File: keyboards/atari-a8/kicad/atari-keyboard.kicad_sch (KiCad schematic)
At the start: 20 parts, among them J101 PLAYER 1, J102 PLAYER 2, J103 I2C DISPLAY, U101 Elite-C

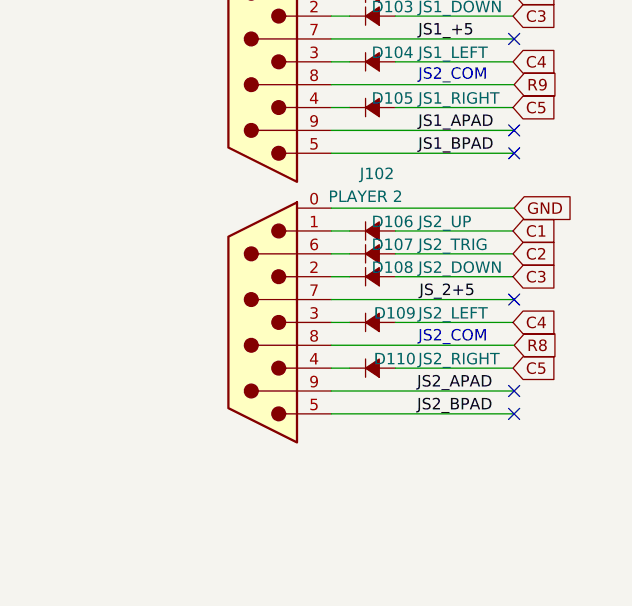
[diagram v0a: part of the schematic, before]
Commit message: Correct key sizes placed, diodes located, various auto-drawn stuff removed from PCB
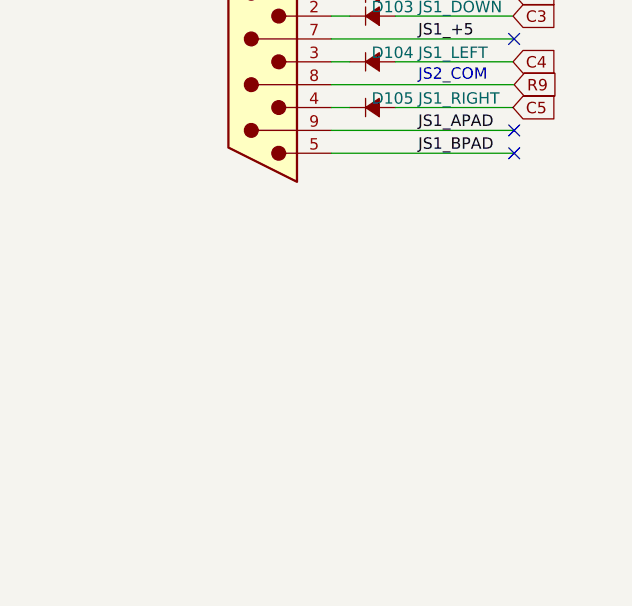
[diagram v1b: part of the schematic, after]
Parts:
- removed D106: JS2_UP, keebio:Diode-dual, symbol atari-keyboard-rescue:D_Small_ALT-Device
- removed D107: JS2_TRIG, retro-kbd:Diode-dual, symbol atari-keyboard-rescue:D_Small_ALT-Device
- removed D108: JS2_DOWN, retro-kbd:Diode-dual, symbol atari-keyboard-rescue:D_Small_ALT-Device
- removed D109: JS2_LEFT, retro-kbd:Diode-dual, symbol atari-keyboard-rescue:D_Small_ALT-Device
- removed D110: JS2_RIGHT, retro-kbd:Diode-dual, symbol atari-keyboard-rescue:D_Small_ALT-Device
- removed J102: PLAYER 2, Connector_Dsub:DSUB-9_Male_Horizontal_P2.77x2.84mm_EdgePinOffset9.90mm_Housed_MountingHolesOffset11.32mm, symbol jsconnector:DB9_Male
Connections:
- no-connect marks 11 -> 8

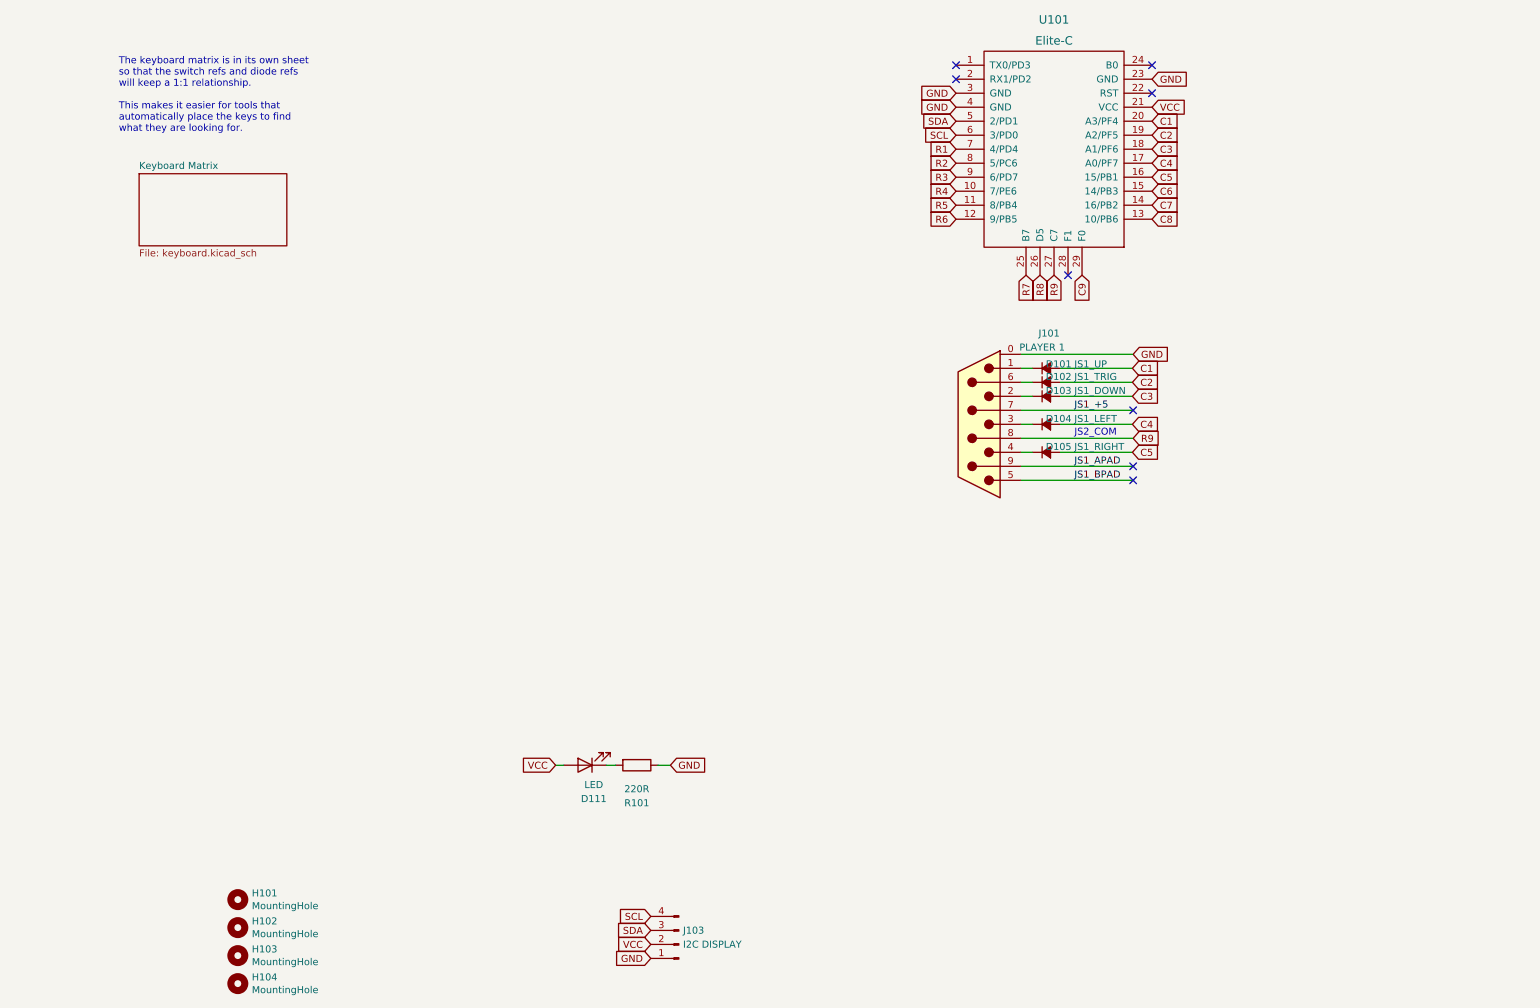
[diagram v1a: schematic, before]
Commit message: All global labels rendered. MAX7219's added. PCB updaed
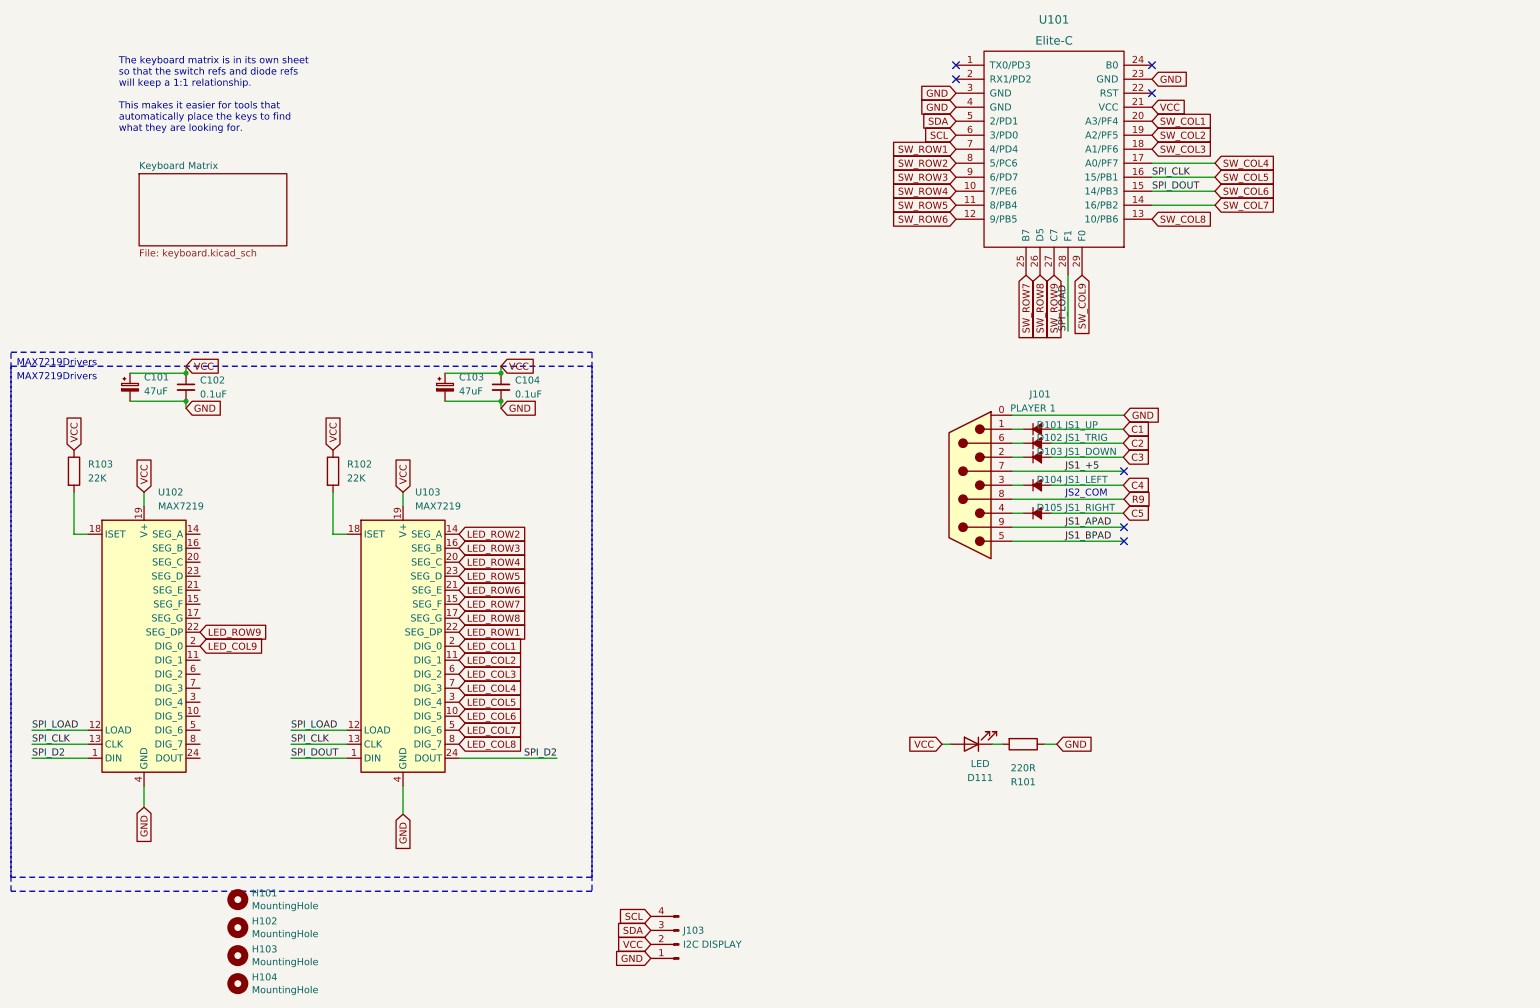
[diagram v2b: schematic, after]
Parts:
- added C101, C103: 47uF, Capacitor_THT:CP_Radial_D5.0mm_P2.50mm, symbol Device:C_Polarized_Small
- added C102, C104: 0.1uF, Capacitor_THT:C_Axial_L3.8mm_D2.6mm_P10.00mm_Horizontal, symbol Device:C_Small
- added R102, R103: 22K, keebio:Resistor-Hybrid, symbol Device:R
- added U102, U103: MAX7219, Package_DIP:DIP-24_W7.62mm_Socket_LongPads, symbol Driver_LED:MAX7219
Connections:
- net C1: no longer U101.20 (A3/PF4)
- net C2: no longer U101.19 (A2/PF5)
- net C3: no longer U101.18 (A1/PF6)
- net C4: no longer U101.17 (A0/PF7)
- net C5: no longer U101.16 (15/PB1)
- net GND: now also C101.2, C102.2, C103.2, C104.2, U102.4 (GND), U102.9 (GND), U103.4 (GND), U103.9 (GND)
- net R9: no longer U101.27 (C7)
- net VCC: now also C101.1, C102.1, C103.1, C104.1, R102.1, R103.1, U102.19 (V+), U103.19 (V+)
- net SPI_LOAD: now reaches U101.28 (F1)
- net SPI_LOAD: now also U102.12 (LOAD), U103.12 (LOAD)
- net C6 renamed SW_COL6
- net SW_COL6: now also U103.1 (DIN)
- net C7 renamed SW_COL7
- net C8 renamed SW_COL8
- net C9 renamed SW_COL9
- net R1 renamed SW_ROW1
- net R2 renamed SW_ROW2
- net R3 renamed SW_ROW3
- net R4 renamed SW_ROW4
- net R5 renamed SW_ROW5
- net R6 renamed SW_ROW6
- net R7 renamed SW_ROW7
- net R8 renamed SW_ROW8
- new net: R102.2, U103.18 (ISET)
- new net: R103.2, U102.18 (ISET)
- new net LED_COL1: U103.2 (DIG_0)
- new net LED_COL2: U103.11 (DIG_1)
- new net LED_COL3: U103.6 (DIG_2)
- new net LED_COL4: U103.7 (DIG_3)
- new net LED_COL5: U103.3 (DIG_4)
- new net LED_COL6: U103.10 (DIG_5)
- new net LED_COL7: U103.5 (DIG_6)
- new net LED_COL8: U103.8 (DIG_7)
- new net LED_COL9: U102.2 (DIG_0)
- new net LED_ROW1: U103.22 (SEG_DP)
- new net LED_ROW2: U103.14 (SEG_A)
- new net LED_ROW3: U103.16 (SEG_B)
- new net LED_ROW4: U103.20 (SEG_C)
- new net LED_ROW5: U103.23 (SEG_D)
- new net LED_ROW6: U103.21 (SEG_E)
- new net LED_ROW7: U103.15 (SEG_F)
- new net LED_ROW8: U103.17 (SEG_G)
- new net LED_ROW9: U102.22 (SEG_DP)
- new net SPI_D2: U102.1 (DIN), U103.24 (DOUT)
- new net SW_COL1: U101.20 (A3/PF4)
- new net SW_COL2: U101.19 (A2/PF5)
- new net SW_COL3: U101.18 (A1/PF6)
- new net SW_COL4: U101.17 (A0/PF7)
- new net SW_COL5: U101.16 (15/PB1), U102.13 (CLK), U103.13 (CLK)
- new net SW_ROW9: U101.27 (C7)
- no-connect marks 8 -> 7
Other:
- moved on the sheet: D101, D102, D103, D104, D105, D111, J101, R101

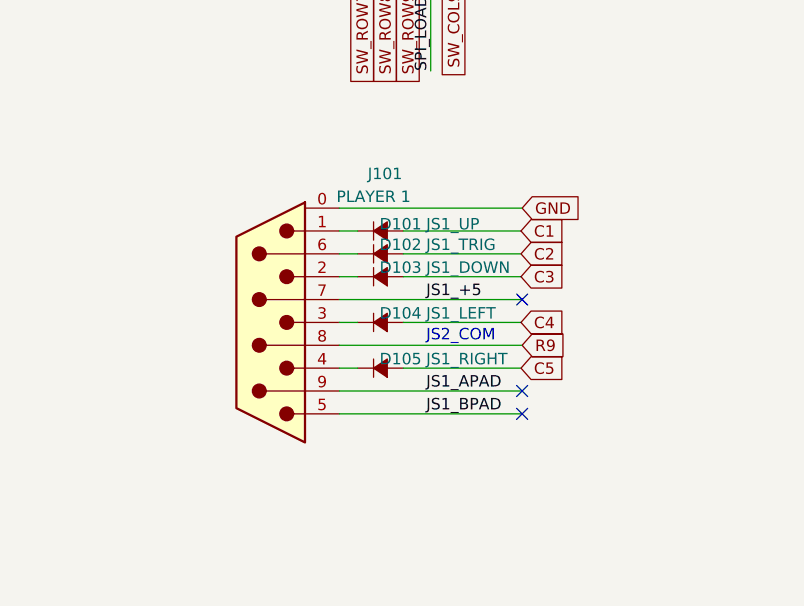
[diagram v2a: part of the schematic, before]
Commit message: Fixed joystick wiring
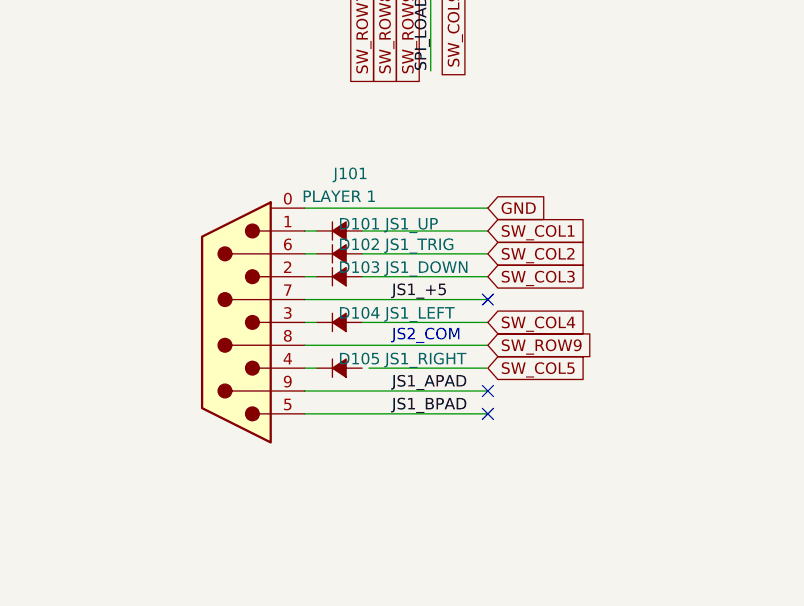
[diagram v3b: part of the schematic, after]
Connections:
- net C1 is gone; now on net SW_COL1: D101.2 (A)
- net C2 is gone; now on net SW_COL2: D102.2 (A)
- net C3 is gone; now on net SW_COL3: D103.2 (A)
- net C4 is gone; now on net SW_COL4: D104.2 (A)
- net R9 is gone; now on net SW_ROW9: J101.8
- net C5: no longer names the net of D105.2 (A)
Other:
- moved on the sheet: D101, D102, D103, D104, D105, J101

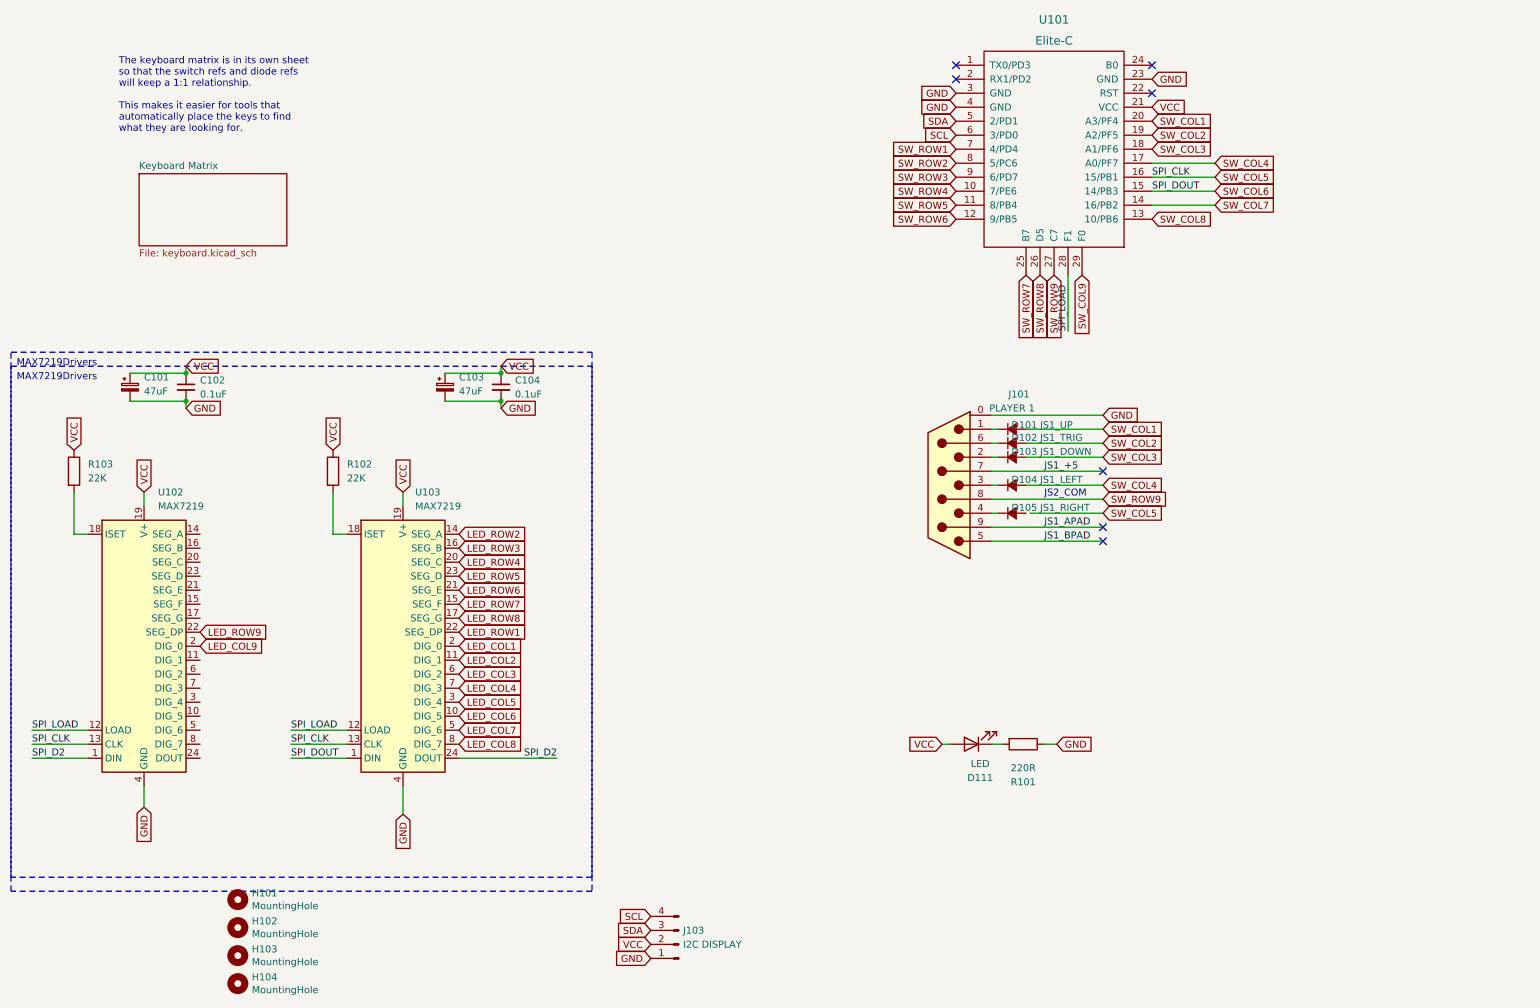
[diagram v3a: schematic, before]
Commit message: Added some tweaks learned working on keyboard prototype
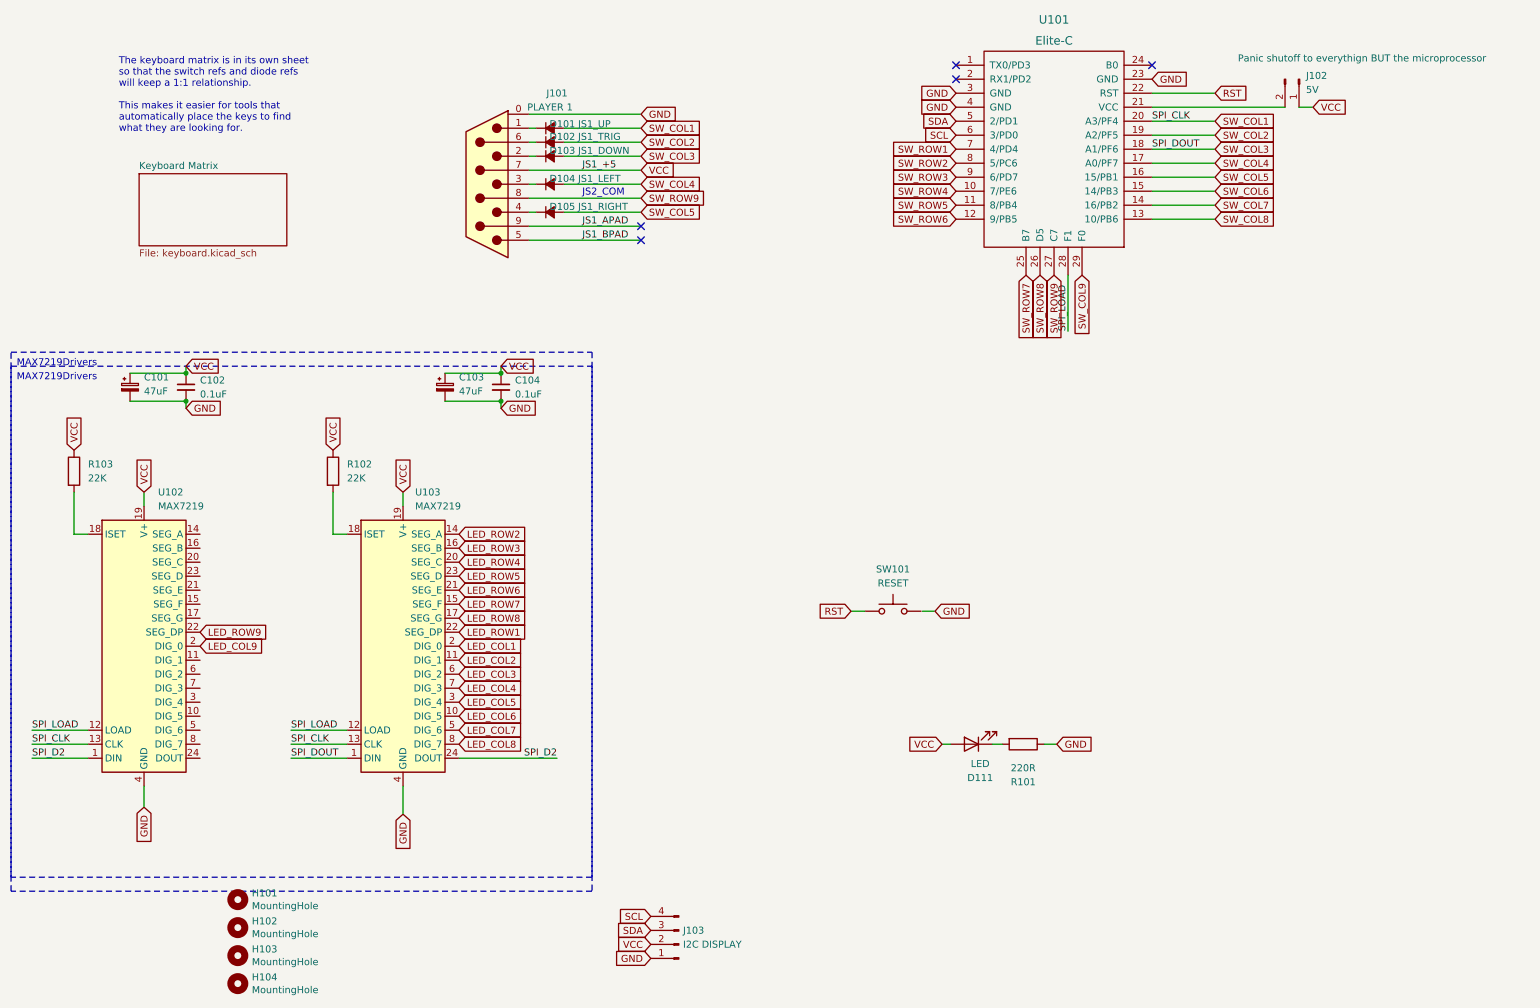
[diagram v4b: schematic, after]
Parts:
- added J102: 5V, Connector_PinHeader_2.54mm:PinHeader_1x02_P2.54mm_Vertical, symbol Connector:Conn_01x02_Pin
- added SW101: RESET, Button_Switch_THT:SW_PUSH_6mm, symbol Switch:SW_Push
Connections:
- net JS1_+5 is gone; now on net VCC: J101.7
- net SW_COL1: now also U102.13 (CLK), U103.13 (CLK)
- net SW_COL3: now also U103.1 (DIN)
- net SW_COL5: now also D105.2 (A); no longer U102.13 (CLK), U103.13 (CLK)
- net SW_COL6: no longer U103.1 (DIN)
- net VCC: now also J102.1 (Pin_1); no longer U101.21 (VCC)
- net RST: now reaches U101.22 (RST)
- net RST: now also SW101.1
- new net: J102.2 (Pin_2), U101.21 (VCC)
- no-connect marks 7 -> 5
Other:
- moved on the sheet: D101, D102, D103, D104, D105, J101
